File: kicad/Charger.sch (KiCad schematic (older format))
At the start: 28 parts, among them P10 USB_A, P11 BAT1, P12 BAT2, P7 USB_A, P8 BAT1, P9 BAT2, U10 MCP73831, U11 MCP73831, U12 MCP73831, U9 MCP73831

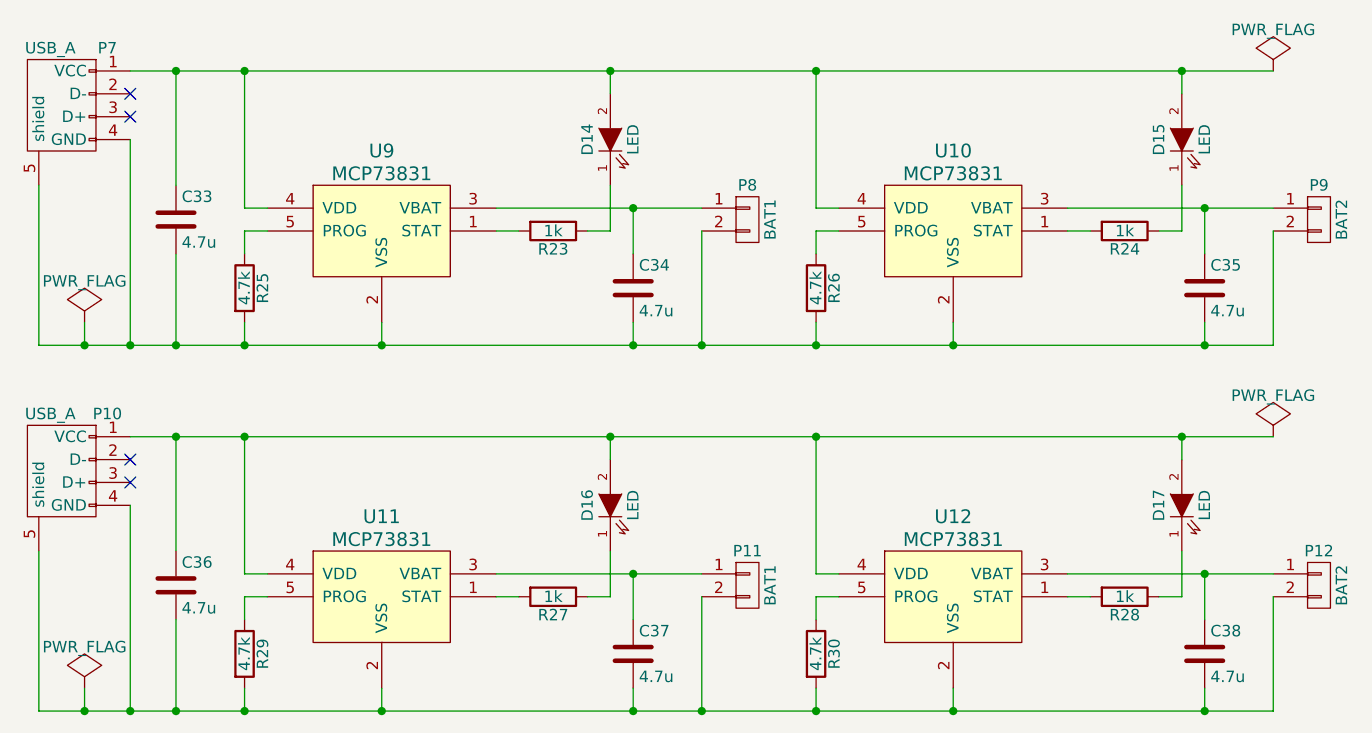
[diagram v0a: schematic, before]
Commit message: 充電基板を階層に．
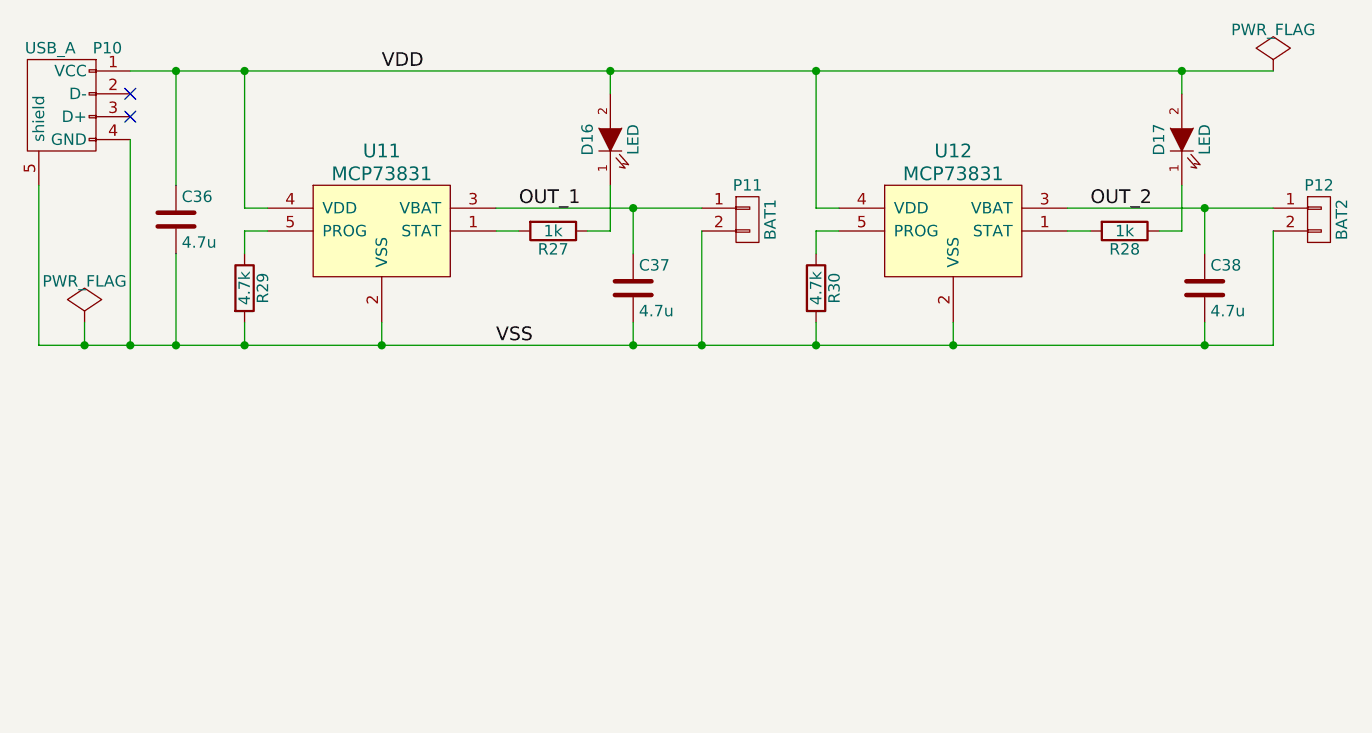
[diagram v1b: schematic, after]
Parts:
- removed C36, C37, C38: 4.7u, Capacitors_SMD:C_0603, symbol C
- removed D16, D17: LED, LEDs:LED_0603, symbol LED
- removed P10: USB_A, mouse:USB_A_P, symbol USB_A
- removed P11: BAT1, Connectors_Hirose:Hirose_DF13-02P-1.25DSA_02x1.25mm_Straight, symbol CONN_01X02
- removed P12: BAT2, Connectors_Hirose:Hirose_DF13-02P-1.25DSA_02x1.25mm_Straight, symbol CONN_01X02
- removed R27, R28: 1k, Resistors_SMD:R_0603, symbol R
- removed R29, R30: 4.7k, Resistors_SMD:R_0603, symbol R
- removed U11, U12: MCP73831, TO_SOT_Packages_SMD:SOT-23-5, symbol MCP73831
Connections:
- net VDD: now reaches C33.1, D14.2 (A), D15.2 (A), P7.1 (VCC), U10.4 (VDD), U9.4 (VDD)
- net VSS: now reaches C33.2, C34.2, C35.2, P7.4 (GND), P7.5 (shield), P8.2 (P2), P9.2 (P2), R25.2, R26.2, U10.2 (VSS), U9.2 (VSS)
- net OUT_2: now reaches C35.1, P9.1 (P1), U10.3 (VBAT)
- net OUT_1: now reaches C34.1, P8.1 (P1), U9.3 (VBAT)
- no-connect marks 4 -> 2
